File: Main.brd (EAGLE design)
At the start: 40.6 x 78.4 mm, 13 parts, among them U1 ESP32-DEVKITC-32D

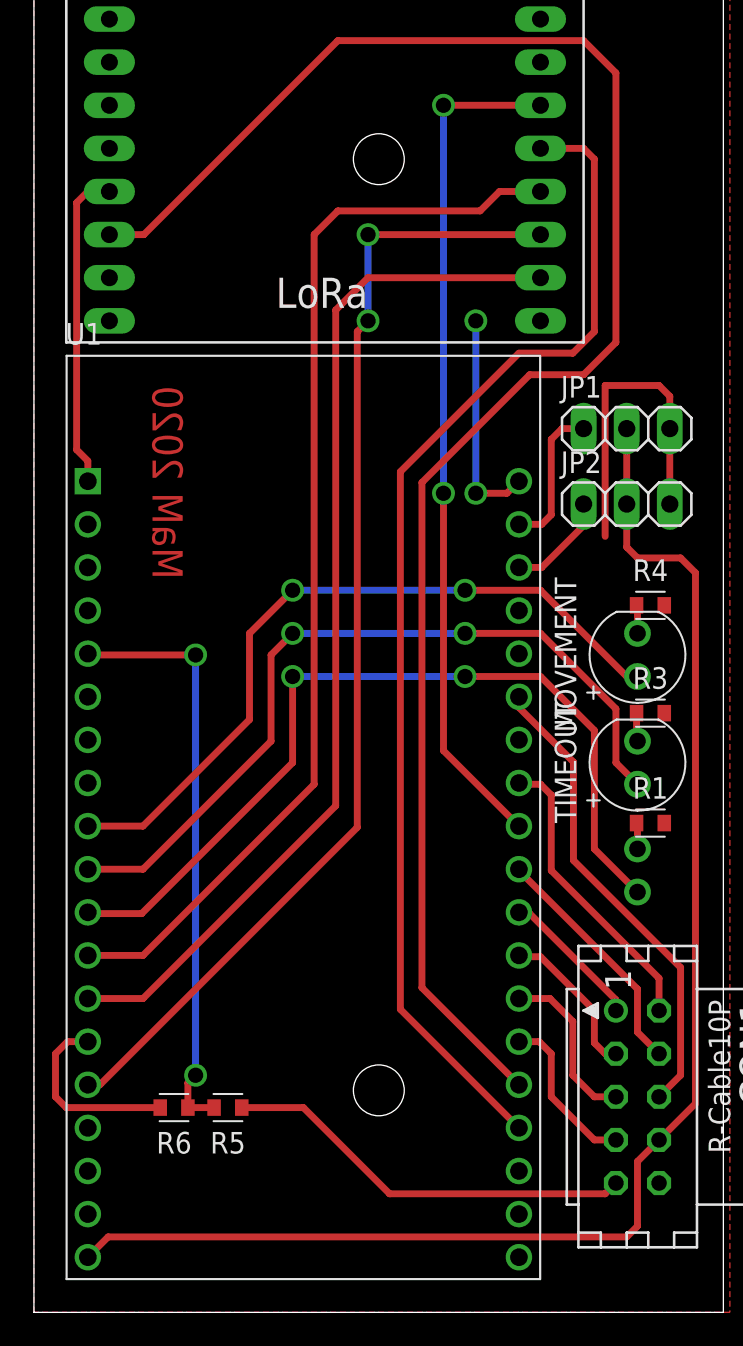
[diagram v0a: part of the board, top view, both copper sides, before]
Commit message: esp32 footprint changed
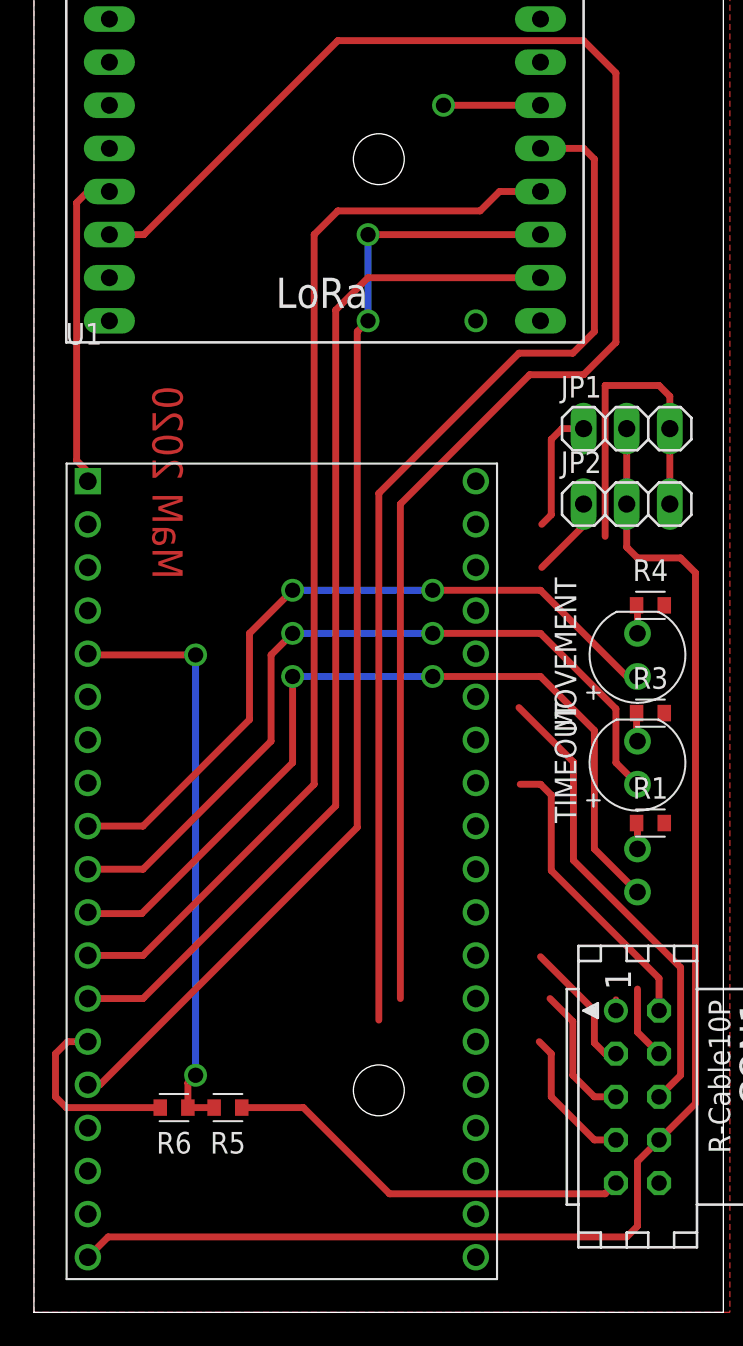
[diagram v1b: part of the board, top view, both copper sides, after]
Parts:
- U1: device ESP32-DEVKITC-32D:MODULE_ESP32-DEVKITC-32D -> custom:MODULE_ESP32-DEVKITC-32D
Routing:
- net LORA_RST: track 50.0 -> 5.71 mm, vias 2 -> 1
- net GND: track 43.5 -> 30.5 mm, vias 2 -> 1
- net M_M2: track 14.3 -> 4.34 mm
- net LORA_CS: track 70.0 -> 61.3 mm
- net M_STEP1: track 8.49 -> 0.63 mm
- net LORA_DIO0: track 103.9 -> 97.0 mm
- net M_STEP2: track 9.97 -> 8.14 mm
- net SERVO_2: track 6.10 -> 4.76 mm
- net SERVO_1: track 8.75 -> 7.40 mm
- net M_DIR1: track 9.23 -> 7.93 mm
- net M_DIR2: track 9.60 -> 8.41 mm
- net M_M0: track 28.0 -> 27.4 mm

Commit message: waiting for review
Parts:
- removed LORA_CONNECTED, MOVEMENT, TIMEOUT: LED_BLUE, Opto-Electronic:LEDRD254W60D565H860B_B
- added LORA, MV, TOUT: LED_BLUE, Opto-Electronic:LEDRD254W60D565H860B_B
- moved CON1 54.0 mm to (34.9, 66.7)
- moved U$3 52.7 mm to (18.2, 13.3), turned to 0 degrees
- moved R5 28.5 mm to (24.1, 37.6), turned to 270 degrees
- moved R6 27.8 mm to (24.1, 34.9), turned to 270 degrees
- moved U1 17.2 mm to (14.6, 46.4), turned to 180 degrees
- moved R1 6.22 mm to (36.3, 22.6)
- moved JP1 5.72 mm to (34.9, 46.4)
- moved R3 5.59 mm to (36.3, 29.7)
- moved R4 5.21 mm to (36.3, 36.4)
- moved JP2 4.45 mm to (34.9, 52.1)
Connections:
- net LORA_CLK: now also U1.28; no longer U1.12
- net LORA_CS: now also U1.29; no longer U1.35
- net LORA_DIO0: now also U1.25; no longer U1.34
- net LORA_LED: now also MV.1, U1.8; no longer MOVEMENT.1, U1.9
- net LORA_MISO: now also U1.27; no longer U1.13
- net LORA_MOSI: now also U1.21; no longer U1.15
- net LORA_RST: now also U1.22; no longer U1.28
- net M_DIR1: now also U1.32; no longer U1.31
- net M_DIR2: now also U1.30; no longer U1.33
- net M_M0: now also U1.13; no longer U1.25
- net M_M1: now also U1.11; no longer U1.27
- net M_M2: now also U1.12; no longer U1.29
- net M_STEP1: now also U1.33; no longer U1.30
- net M_STEP2: now also U1.31; no longer U1.32
- net N$1: now also TOUT.2; no longer TIMEOUT.2
- net N$2: now also MV.2; no longer MOVEMENT.2
- net N$3: now also LORA.2; no longer LORA_CONNECTED.2
- net SERVO_1: now also U1.9; no longer U1.21
- net SERVO_2: now also U1.10; no longer U1.22
- net TIMEOUT_LED: now also TOUT.1, U1.7; no longer TIMEOUT.1, U1.10
- net WS_LED: now also LORA.1, U1.6; no longer LORA_CONNECTED.1, U1.11
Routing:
- net LORA_MOSI: track 67.5 -> 18.4 mm
- net 6V: track 84.7 -> 37.2 mm, vias 0 -> 2
- net LORA_DIO0: track 97.0 -> 49.6 mm, vias 0 -> 4
- net M_STEP1: track 0.63 -> 34.8 mm
- net LORA_LED: track 43.2 -> 9.47 mm, vias 2 -> 0
- net TIMEOUT_LED: track 46.7 -> 13.5 mm, vias 2 -> 0
- net LORA_RST: track 5.71 -> 38.5 mm, vias 1 -> 2
- net WS_LED: track 50.5 -> 17.8 mm, vias 2 -> 0
- net LORA_MISO: track 62.0 -> 30.7 mm
- net ADC_BAT: track 34.8 -> 4.22 mm, vias 2 -> 0
- net M_DIR1: track 7.93 -> 36.0 mm
- net M_STEP2: track 8.14 -> 34.2 mm
- net M_DIR2: track 8.41 -> 34.2 mm
- net LORA_CLK: track 64.3 -> 40.8 mm
- net GND: track 30.5 -> 7.51 mm, vias 1 -> 2
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
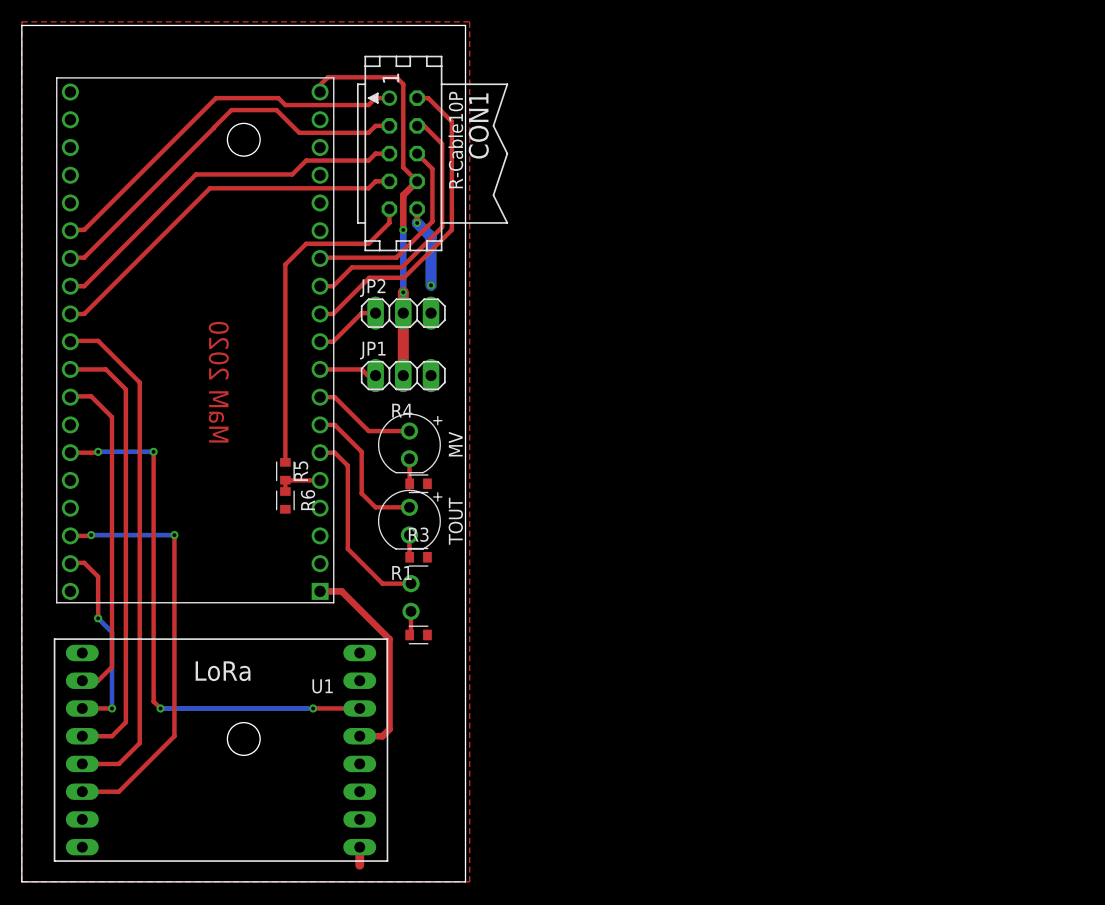
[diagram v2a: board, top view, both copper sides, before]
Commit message: panel size fixed, fixing points added
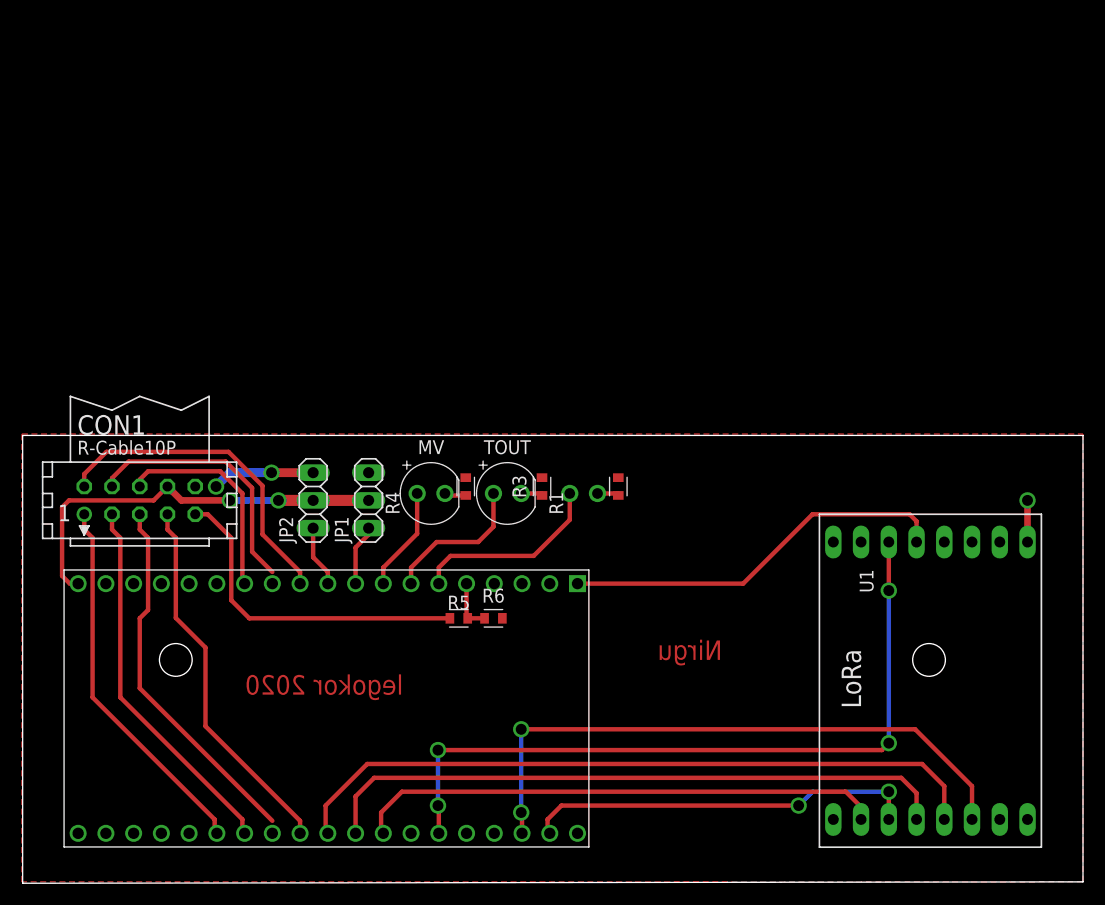
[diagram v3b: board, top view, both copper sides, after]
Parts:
- moved U$3 63.9 mm to (81.9, 18.4), turned to 90 degrees
- moved CON1 39.9 mm to (10.8, 34.9), turned to 0 degrees
- moved U1 35.8 mm to (31.1, 14.6), turned to 270 degrees
- moved R1 22.8 mm to (54.6, 36.2), turned to 90 degrees
- moved R6 21.9 mm to (43.2, 24.1), turned to 0 degrees
- moved R5 20.8 mm to (40.0, 24.1), turned to 0 degrees
- moved JP2 19.0 mm to (26.7, 34.9), turned to 90 degrees
- moved LORA 18.5 mm to (51.4, 35.6), turned to 180 degrees
- moved R3 13.0 mm to (47.6, 36.2), turned to 90 degrees
- moved JP1 11.9 mm to (31.8, 34.9), turned to 90 degrees
- moved TOUT 9.32 mm to (44.5, 35.6), turned to 0 degrees
- moved MV 4.86 mm to (37.5, 35.6), turned to 0 degrees
- moved R4 4.33 mm to (40.6, 36.2), turned to 90 degrees
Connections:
- net M_DIR1: now also CON1.4, U1.12; no longer CON1.3, U1.32
- net M_M0: now also CON1.5, U1.31; no longer CON1.6, U1.13
- net M_M1: now also CON1.3, U1.32; no longer CON1.2, U1.11
- net M_M2: now also CON1.1, U1.33; no longer CON1.4, U1.12
- net M_STEP1: now also CON1.2, U1.11; no longer CON1.1, U1.33
- net M_STEP2: now also CON1.6, U1.13; no longer CON1.5, U1.31
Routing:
- net LORA_DIO0: track 49.6 -> 67.6 mm
- net LORA_MOSI: track 18.4 -> 36.2 mm
- net 3V3: track 19.4 -> 37.1 mm
- net LORA_CS: track 47.0 -> 64.7 mm
- net LORA_MISO: track 30.7 -> 48.4 mm
- net LORA_CLK: track 40.8 -> 58.4 mm
- net LORA_RST: track 38.5 -> 56.0 mm
- net M_M0: track 18.5 -> 33.7 mm
- net M_STEP2: track 34.2 -> 19.5 mm
- net M_DIR1: track 36.0 -> 23.7 mm
- net M_M2: track 24.0 -> 34.2 mm
- net M_M1: track 29.2 -> 34.2 mm
- net M_STEP1: track 34.8 -> 30.0 mm
- net ANTENNA: track 1.65 -> 3.81 mm, vias 0 -> 1
- net GND: track 7.51 -> 9.42 mm
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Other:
- board size 40.6 x 78.4 mm -> 97.1 x 41 mm
- board text added: "Nirgu"
- board text added: "legokor 2020"
- board text removed: "MaM 2020"
